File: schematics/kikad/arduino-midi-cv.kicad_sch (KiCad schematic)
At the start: 72 parts, among them J1 Velocity, J2 GATE OUT, J3 Bend Out, J4 MOD WHEEL, J5 V/oct OUT, J6 Power connector, J7 Eurorack power connector, Q1 BC548, Q2 BC548, SW1 RotaryEncoder_Switch, U1 TL074, U2 6N137, U3 OLED_Display_SPI

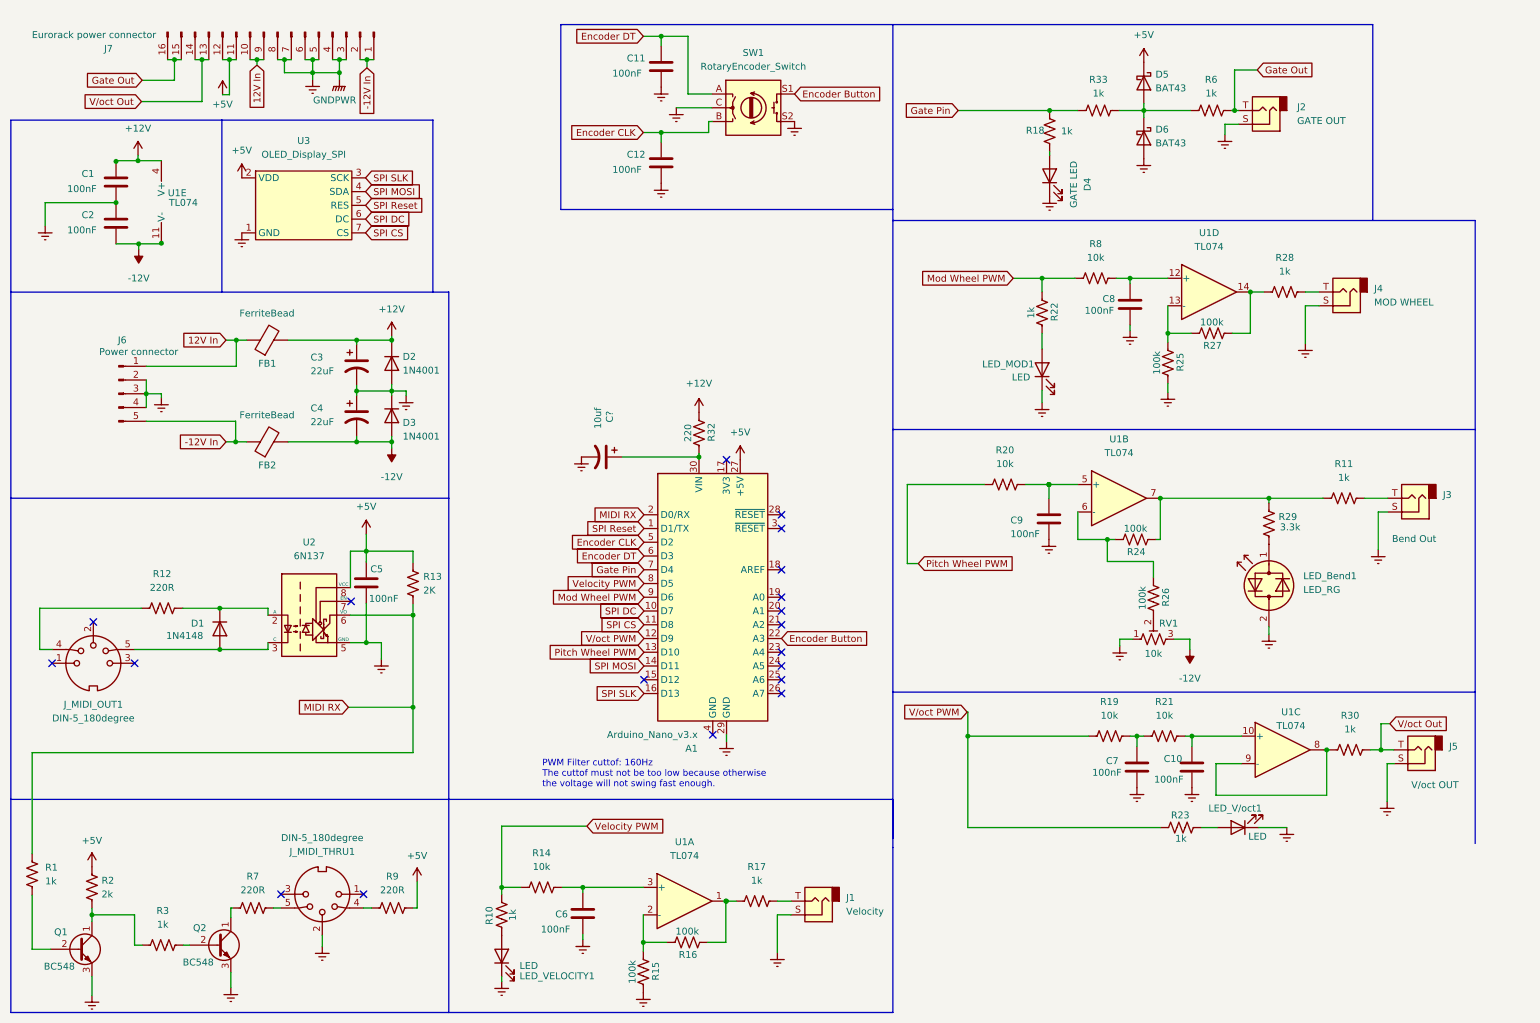
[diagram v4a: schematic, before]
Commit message: Add DAC to shematic (untested)
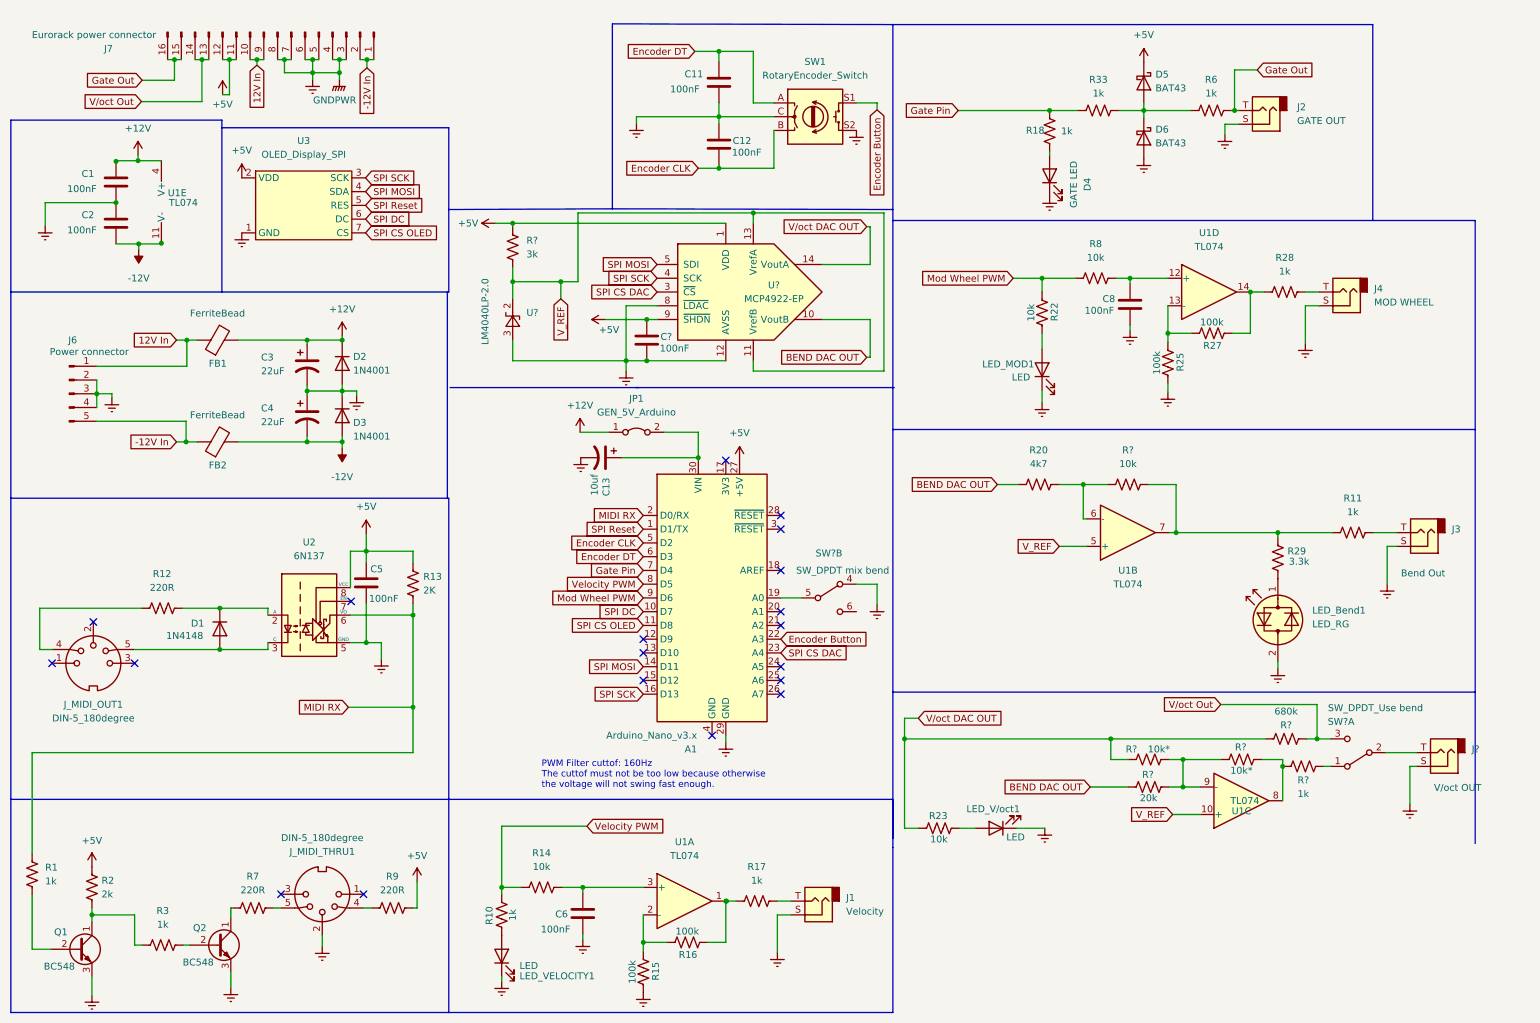
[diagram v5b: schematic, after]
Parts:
- removed C10, C7, C9: 100nF, Capacitor_THT:C_Disc_D3.0mm_W1.6mm_P2.50mm, symbol Device:C
- removed J5: V/oct OUT, Library:Jack breakcout cables, symbol Connector:AudioJack2
- removed R19, R21: 10k, Resistor_THT:R_Axial_DIN0207_L6.3mm_D2.5mm_P10.16mm_Horizontal, symbol Device:R_US
- removed R24: 100k, Resistor_THT:R_Axial_DIN0207_L6.3mm_D2.5mm_P2.54mm_Vertical, symbol Device:R_US
- removed R26: 100k, Resistor_THT:R_Axial_DIN0207_L6.3mm_D2.5mm_P10.16mm_Horizontal, symbol Device:R_US
- removed R30: 1k, Resistor_THT:R_Axial_DIN0207_L6.3mm_D2.5mm_P10.16mm_Horizontal, symbol Device:R_US
- removed R32: 220, Resistor_SMD:R_0805_2012Metric_Pad1.20x1.40mm_HandSolder, symbol Device:R_US
- removed RV1: 10k, Potentiometer_THT:Potentiometer_Bourns_3296W_Vertical, symbol Device:R_Potentiometer_Trim_US
- added C?: 100nF, Capacitor_THT:C_Disc_D3.0mm_W1.6mm_P2.50mm, symbol Device:C
- added J?: V/oct OUT, Library:Jack breakcout cables, symbol Connector:AudioJack2
- added JP1: GEN_5V_Arduino, Jumper:SolderJumper-2_P1.3mm_Open_RoundedPad1.0x1.5mm, symbol Jumper:Jumper_2_Bridged
- added R? (x2): 10k*, Resistor_THT:R_Axial_DIN0207_L6.3mm_D2.5mm_P10.16mm_Horizontal, symbol Device:R_US
- added R?: 680k, Resistor_THT:R_Axial_DIN0207_L6.3mm_D2.5mm_P10.16mm_Horizontal, symbol Device:R_US
- added R?: 10k, Resistor_THT:R_Axial_DIN0207_L6.3mm_D2.5mm_P10.16mm_Horizontal, symbol Device:R_US
- added R?: 1k, Resistor_THT:R_Axial_DIN0207_L6.3mm_D2.5mm_P10.16mm_Horizontal, symbol Device:R_US
- added R?: 3k, Resistor_THT:R_Axial_DIN0207_L6.3mm_D2.5mm_P10.16mm_Horizontal, symbol Device:R_US
- added R?: 20k, Resistor_THT:R_Axial_DIN0207_L6.3mm_D2.5mm_P10.16mm_Horizontal, symbol Device:R_US
- added SW?: SW_DPDT mix bend, symbol Switch:SW_DPDT_x2
- added SW?: SW_DPDT_Use bend, symbol Switch:SW_DPDT_x2
- added U?: LM4040LP-2.0, Package_TO_SOT_THT:TO-92_Inline, symbol Reference_Voltage:LM4040LP-2.0
- added U?: MCP4922-EP, symbol Analog_DAC:MCP4922-EP
- R20: value 10k -> 4k7
- R22, R23: value 1k -> 10k
- gave numbers to parts that had none: 1
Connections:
- net +12V: now also JP1.1 (A)
- net +5V: now also C?.1, R?.2, U?.1 (VDD), U?.9 (~{SHDN})
- net Earth: now also C12.1, C?.2, J?.S, SW?.4 (A), U?.12 (AVSS), U?.3 (A), U?.8 (~{LDAC}); no longer C12.2
- net Encoder CLK: now also C12.2; no longer C12.1
- net SPI MOSI: now also U?.5 (SDI)
- net V/oct  Out: now also R?.1, SW?.3 (C)
- net V_REF: now reaches U1.10 (+)
- net V_REF: now also U1.5 (+), R?.1, U?.11 (VrefB), U?.13 (VrefA), U?.2 (K)
- net at U1.8: now also R?.1, R?.1; no longer U1.9 (-)
- net at A1.30 (VIN), C13.1: now also JP1.2 (B)
- net at R20.2: now also U1.6 (-), R?.1; no longer U1.5 (+)
- net at R11.1, R29.1, U1.7: now also R?.2
- net at A1.19 (A0): now also SW?.5 (B)
- net SPI CS DAC: now reaches A1.23 (A4)
- net SPI CS DAC: now also U?.3 (~{CS})
- net Pitch Wheel PWM: no longer names the net of A1.13 (D10)
- net Pitch Wheel PWM: no longer R20.1
- net SPI CS renamed SPI CS OLED
- net SPI SLK renamed SPI SCK
- net SPI SCK: now also U?.4 (SCK)
- net V/oct PWM: no longer names the net of A1.12 (D9)
- net V/oct PWM: no longer R23.2
- new net: R?.1, R?.1, R?.2, U1.9 (-)
- new net: J?.T, SW?.2 (B)
- new net: R?.2, SW?.1 (A)
- new net BEND DAC OUT: R20.1, R?.2, U?.10 (VoutB)
- new net V/oct DAC OUT: R23.2, R?.2, R?.2, U?.14 (VoutA)
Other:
- moved on the sheet: C11, C12, C3, C4, D2, D3, FB1, FB2, J3, J6, LED_Bend1, LED_V/oct1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

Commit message: Change indentation to tabs. To HELL with spaces!
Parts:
- gave numbers to parts that had none: 13
